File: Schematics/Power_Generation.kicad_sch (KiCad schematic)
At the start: 21 parts, among them U3 LMR36520ADDAR, U7 TLV75733PDRV

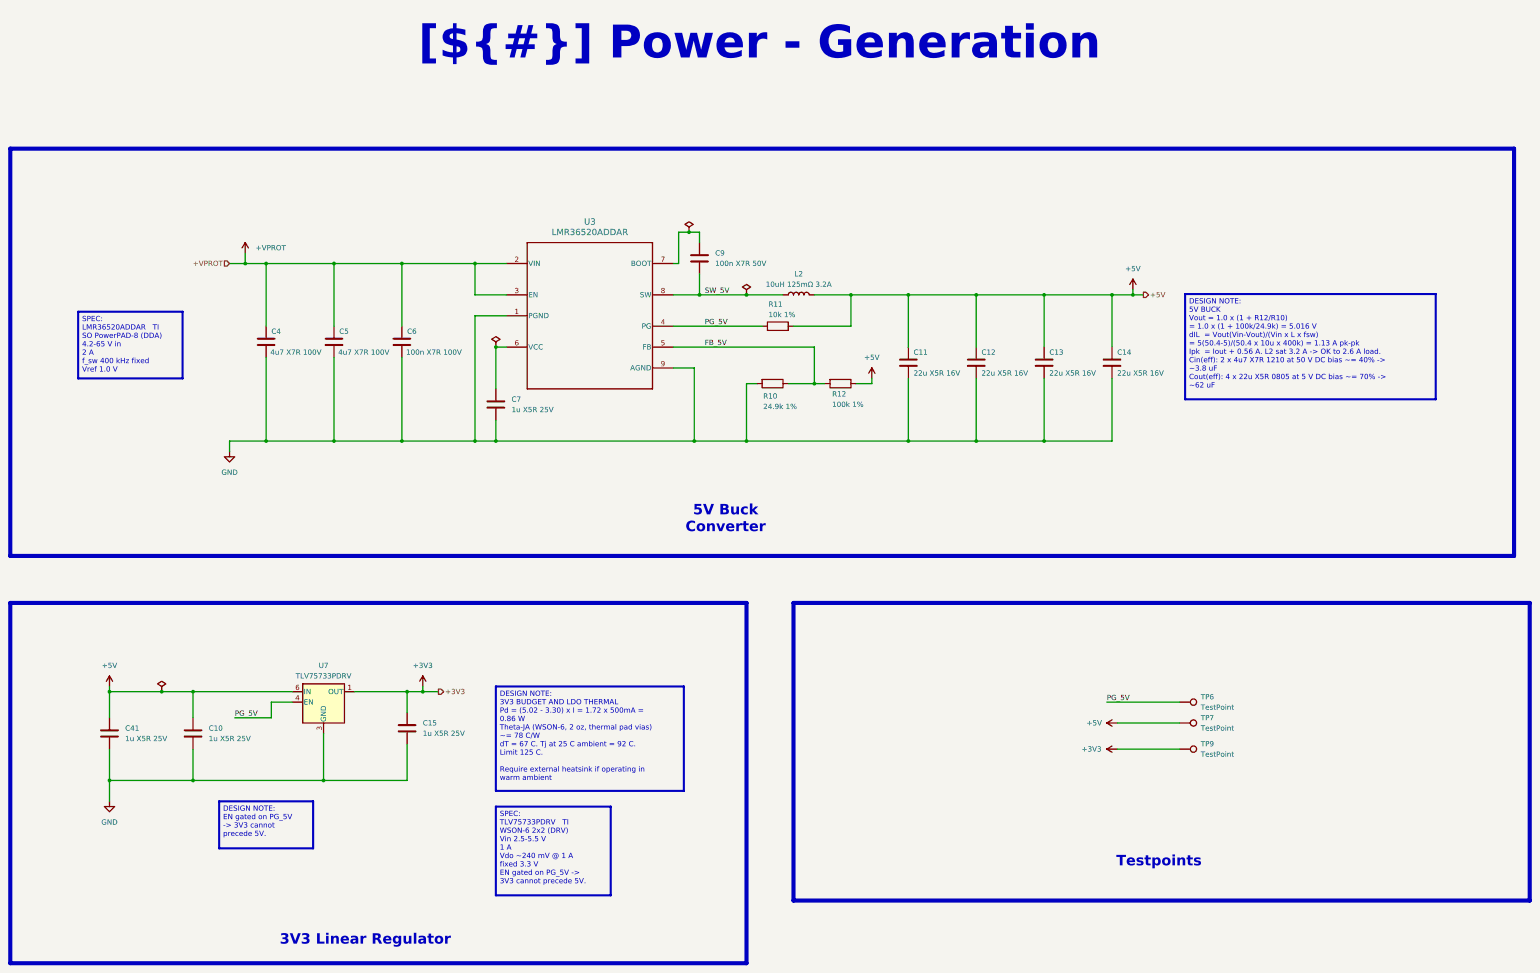
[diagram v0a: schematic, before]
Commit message: Clean up schematic design notes; export schematic and PCB artwork PDFs
- Remove firmware-only notes (boot sequence, calibration procedure,
  firmware SPI/PWM settings) and template/empty text; keep hardware facts
- Tighten wording of all DESIGN/SPEC/ASSEMBLY/REV 1 notes and resize
  boxes so no note text wraps or overflows
- Re-export schematic PDF
- Add PCB artwork PDFs (combined and one per layer: silk, paste, mask,
  L1-L6 copper), board outline on every page

Co-Authored-By: Claude Opus 5.5 <noreply@anthropic.com>
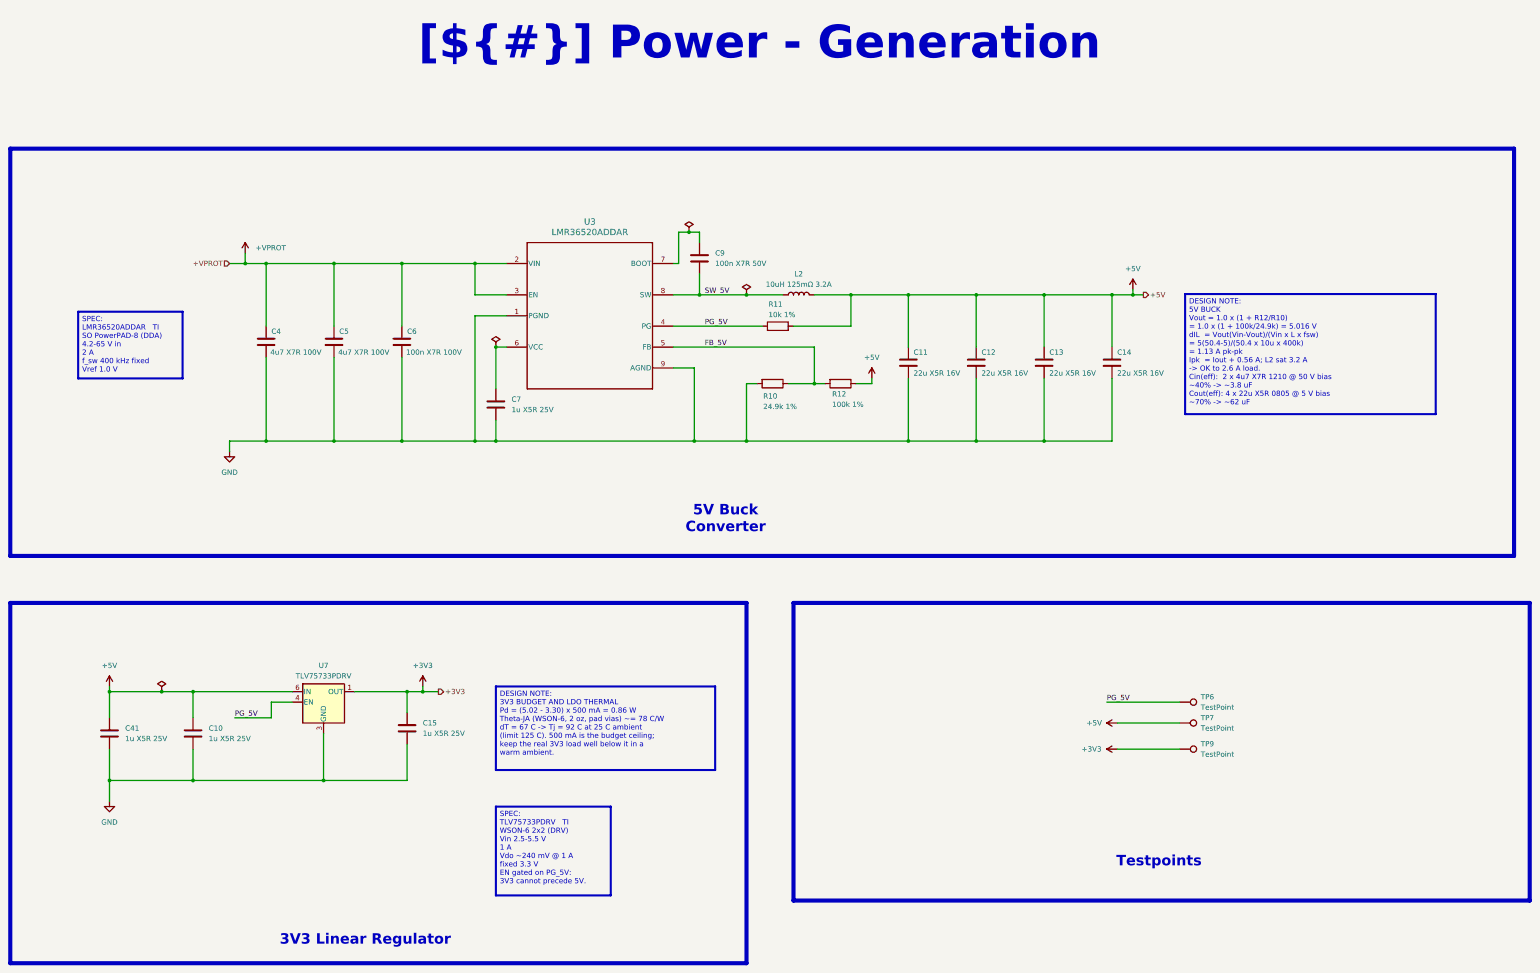
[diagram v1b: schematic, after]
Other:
- company: (none) -> ${COMPANY}
- title: (none) -> Power - Generation
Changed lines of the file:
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@@
 	(generator_version "10.0")
 	(paper "A3")
+	(title_block
+		(title "Power - Generation")
+		(date "${RELEASE_DATE}")
+		(rev "${REVISION}")
+		(company "${COMPANY}")
+	)
 	(rectangle
 		(start 27.94 161.29)
@@
 		)
 	)
-	(text_box "SPEC:\nTLV75733PDRV   TI   \nWSON-6 2x2 (DRV)\nVin 2.5-5.5 V \n1 A \nVdo ~240 mV @ 1 A \nfixed 3.3 V\nEN gated on PG_5V -> 3V3 cannot precede 5V."
+	(text_box "SPEC:\nTLV75733PDRV   TI\nWSON-6 2x2 (DRV)\nVin 2.5-5.5 V\n1 A\nVdo ~240 mV @ 1 A\nfixed 3.3 V\nEN gated on PG_5V:\n3V3 cannot precede 5V."
 		(exclude_from_sim no)
 		(at 146.05 210.8347 0)
-		(size 27.94 21.5753)
+		(size 27.94 21.59)
 		(margins 0.9525 0.9525 0.9525 0.9525)
 		(stroke
@@
 		)
 	)
-	(text_box "DESIGN NOTE:\nEN gated on PG_5V -> 3V3 cannot precede 5V."
-		(exclude_from_sim no)
-		(at 78.74 209.55 0)
-		(size 22.86 11.43)
-		(margins 0.9525 0.9525 0.9525 0.9525)
-		(stroke
-			(width 0.508)
-			(type solid)
-			(color 0 0 255 1)
-		)
-		(fill
-			(type color)
-			(color 255 255 255 1)
-		)
-		(effects
-			(font
-				(size 1.27 1.27)
-				(color 0 0 0 1)
-			)
-			(justify left top)
-		)
-	)
-	(text_box "DESIGN NOTE:\n5V BUCK\nVout = 1.0 x (1 + R12/R10) \n     = 1.0 x (1 + 100k/24.9k) = 5.016 V\ndIL  = Vout(Vin-Vout)/(Vin x L x fsw)\n     = 5(50.4-5)/(50.4 x 10u x 400k) = 1.13 A pk-pk\nIpk  = Iout + 0.56 A. L2 sat 3.2 A -> OK to 2.6 A load.\nCin(eff): 2 x 4u7 X7R 1210 at 50 V DC bias ~= 40% -> ~3.8 uF\nCout(eff): 4 x 22u X5R 0805 at 5 V DC bias ~= 70% -> ~62 uF"
+	(text_box "DESIGN NOTE:\n5V BUCK\nVout = 1.0 x (1 + R12/R10)\n     = 1.0 x (1 + 100k/24.9k) = 5.016 V\ndIL  = Vout(Vin-Vout)/(Vin x L x fsw)\n     = 5(50.4-5)/(50.4 x 10u x 400k)\n     = 1.13 A pk-pk\nIpk  = Iout + 0.56 A; L2 sat 3.2 A\n     -> OK to 2.6 A load.\nCin(eff):  2 x 4u7 X7R 1210 @ 50 V bias\n           ~40% -> ~3.8 uF\nCout(eff): 4 x 22u X5R 0805 @ 5 V bias\n           ~70% -> ~62 uF"
 		(exclude_from_sim no)
 		(at 313.69 86.1587 0)
-		(size 60.96 25.6013)
-		(margins 0.9525 0.9525 0.9525 0.9525)
-		(stroke
-			(width 0.508)
-			(type solid)
-			(color 0 0 255 1)
-		)
-		(fill
-			(type color)
-			(color 255 255 255 1)
-		)
-		(effects
-			(font
-				(size 1.27 1.27)
-				(color 0 0 0 1)
-			)
-			(justify left top)
-		)
-	)
-	(text_box "DESIGN NOTE:\n3V3 BUDGET AND LDO THERMAL\nPd = (5.02 - 3.30) x I = 1.72 x 500mA = 0.86 W\nTheta-JA (WSON-6, 2 oz, thermal pad vias) ~= 78 C/W\ndT = 67 C. Tj at 25 C ambient = 92 C. Limit 125 C.\n\nRequire external heatsink if operating in warm ambient"
-		(exclude_from_sim no)
-		(at 146.05 181.6101 0)
-		(size 45.72 25.3999)
+		(size 60.96 29.21)
 		(margins 0.9525 0.9525 0.9525 0.9525)
 		(stroke
@@
 		)
 	)
-)
+	(text_box "DESIGN NOTE:\n3V3 BUDGET AND LDO THERMAL\nPd = (5.02 - 3.30) x 500 mA = 0.86 W\nTheta-JA (WSON-6, 2 oz, pad vias) ~= 78 C/W\ndT = 67 C -> Tj = 92 C at 25 C ambient\n(limit 125 C). 500 mA is the budget ceiling;\nkeep the real 3V3 load well below it in a\nwarm ambient."
+		(exclude_from_sim no)
+		(at 146.05 181.6101 0)
+		(size 53.34 20.32)
+		(margins 0.9525 0.9525 0.9525 0.9525)
+		(stroke
+			(width 0.508)
+			(type solid)
+			(color 0 0 255 1)
+		)
+		(fill
+			(type color)
+			(color 255 255 255 1)
+		)
+		(effects
+			(font
+				(size 1.27 1.27)
+				(color 0 0 0 1)
+			)
+			(justify left top)
+		)
+	))
